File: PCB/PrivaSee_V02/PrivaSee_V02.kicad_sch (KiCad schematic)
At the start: 35 parts, among them J1 RFPC-SMA27-F, J2 Batt_Solder_Point, J3 Conn_02x06_Odd_Even, J4 VOUT_TEST, J5 GND_TEST, J6 IR_TEST, J7 RF_TEST, SW1 Switch, U1 RC1602A, U2 LM358, U3 254, U4 DFR0568, U6 ESP32-C5-DevKitC-1

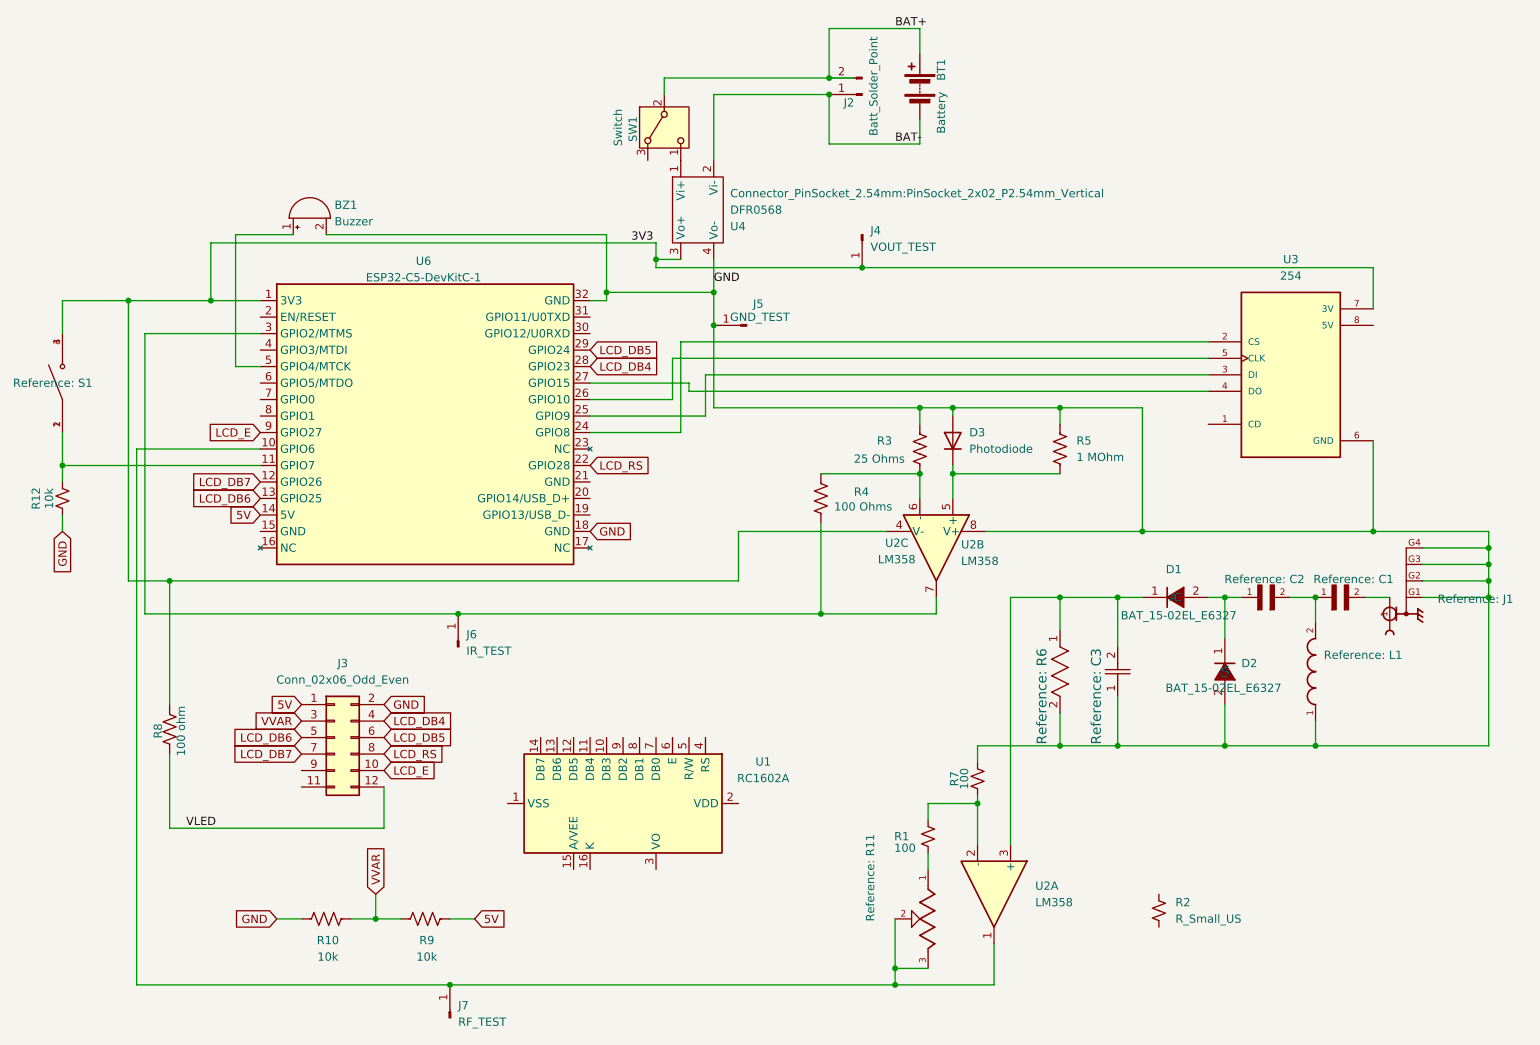
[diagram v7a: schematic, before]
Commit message: LM358 change
Our current schematic has the symbols for V- and V+ swapped. Ground and power are now routed and traced properly
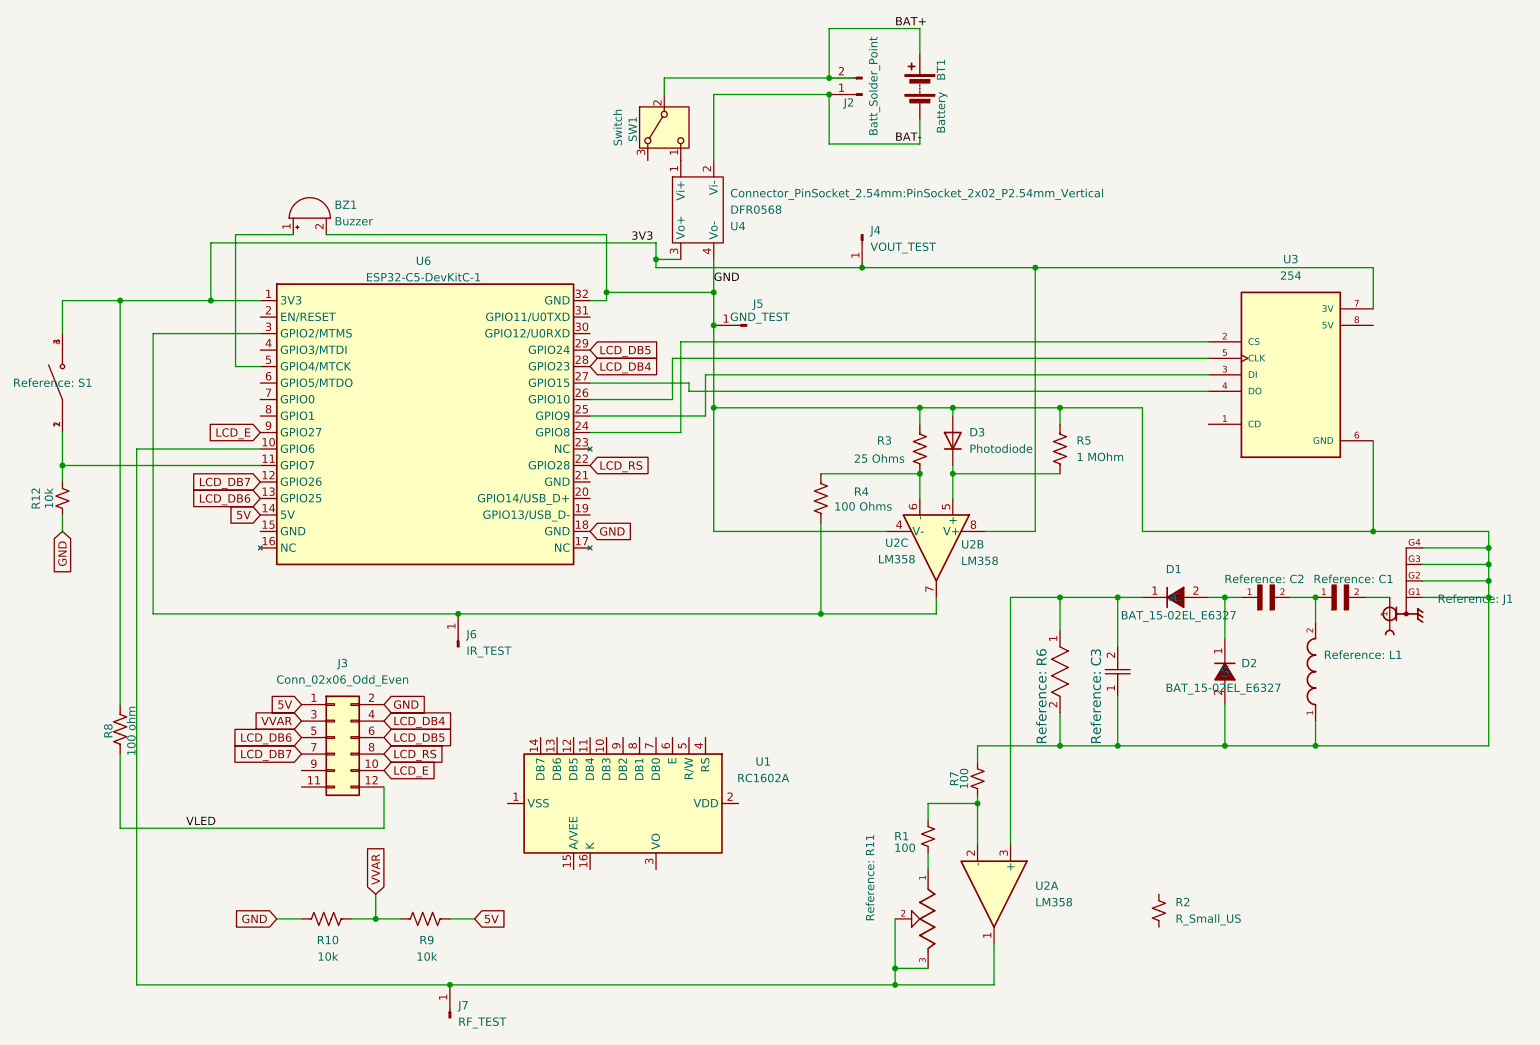
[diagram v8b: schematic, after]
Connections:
- net 3V3: now also U2.8 (V+); no longer U2.4 (V-)
- net GND: now also U2.4 (V-); no longer U2.8 (V+)
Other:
- moved on the sheet: R8
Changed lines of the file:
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@@
 	)
 	(junction
-		(at 95.25 105.41)
-		(diameter 0)
-		(color 0 0 0 0)
-	)
-	(junction
 		(at 118.11 55.88)
 		(diameter 0)
@@
 	)
 	(junction
-		(at 50.8 100.33)
-		(diameter 0)
-		(color 0 0 0 0)
-	)
-	(junction
 		(at 236.22 92.71)
 		(diameter 0)
@@
 	)
 	(junction
-		(at 151.13 105.41)
+		(at 184.15 52.07)
 		(diameter 0)
 		(color 0 0 0 0)
 	)
 	(junction
-		(at 152.4 25.4)
+		(at 151.13 105.41)
 		(diameter 0)
 		(color 0 0 0 0)
 	)
 	(junction
-		(at 200.66 92.71)
+		(at 152.4 25.4)
 		(diameter 0)
 		(color 0 0 0 0)
@@
 	)
 	(junction
-		(at 44.45 57.15)
+		(at 134.62 73.66)
 		(diameter 0)
 		(color 0 0 0 0)
@@
 	)
 	(junction
+		(at 43.18 57.15)
+		(diameter 0)
+		(color 0 0 0 0)
+	)
+	(junction
 		(at 162.56 160.02)
 		(diameter 0)
@@
 	)
 	(junction
+		(at 95.25 105.41)
+		(diameter 0)
+		(color 0 0 0 0)
+	)
+	(junction
 		(at 213.36 125.73)
 		(diameter 0)
@@
 	(wire
 		(pts
-			(xy 44.45 57.15) (xy 44.45 100.33)
+			(xy 43.18 57.15) (xy 43.18 119.38)
 		)
 		(stroke
@@
 	(wire
 		(pts
-			(xy 46.99 62.23) (xy 46.99 105.41)
+			(xy 184.15 92.71) (xy 176.53 92.71)
 		)
 		(stroke
@@
 	(wire
 		(pts
-			(xy 157.48 52.07) (xy 236.22 52.07)
+			(xy 48.26 62.23) (xy 48.26 105.41)
+		)
+		(stroke
+			(width 0)
+			(type default)
+		)
+	)
+	(wire
+		(pts
+			(xy 157.48 52.07) (xy 184.15 52.07)
 		)
 		(stroke
@@
 	(wire
 		(pts
-			(xy 213.36 102.87) (xy 215.9 102.87)
+			(xy 184.15 52.07) (xy 236.22 52.07)
 		)
 		(stroke
@@
 	(wire
 		(pts
-			(xy 34.29 57.15) (xy 34.29 62.23)
+			(xy 213.36 102.87) (xy 215.9 102.87)
 		)
 		(stroke
@@
 	(wire
 		(pts
-			(xy 175.26 125.73) (xy 175.26 128.27)
+			(xy 34.29 57.15) (xy 34.29 62.23)
 		)
 		(stroke
@@
 	(wire
 		(pts
-			(xy 44.45 100.33) (xy 138.43 100.33)
+			(xy 175.26 125.73) (xy 175.26 128.27)
 		)
 		(stroke
@@
 	(wire
 		(pts
-			(xy 138.43 100.33) (xy 138.43 92.71)
-		)
-		(stroke
-			(width 0)
-			(type default)
-		)
-	)
-	(wire
-		(pts
 			(xy 83.82 138.43) (xy 83.82 132.08)
 		)
@@
 	(wire
 		(pts
-			(xy 50.8 138.43) (xy 50.8 127)
-		)
-		(stroke
-			(width 0)
-			(type default)
-		)
-	)
-	(wire
-		(pts
-			(xy 46.99 105.41) (xy 95.25 105.41)
+			(xy 43.18 138.43) (xy 43.18 127)
 		)
 		(stroke
@@
 	(wire
 		(pts
-			(xy 50.8 100.33) (xy 50.8 119.38)
+			(xy 48.26 105.41) (xy 95.25 105.41)
 		)
 		(stroke
@@
 	(wire
 		(pts
-			(xy 46.99 62.23) (xy 64.77 62.23)
+			(xy 184.15 52.07) (xy 184.15 92.71)
 		)
 		(stroke
@@
 	(wire
 		(pts
-			(xy 82.55 148.59) (xy 82.55 152.4)
+			(xy 48.26 62.23) (xy 64.77 62.23)
 		)
 		(stroke
@@
 	(wire
 		(pts
-			(xy 130.81 69.85) (xy 115.57 69.85)
+			(xy 82.55 148.59) (xy 82.55 152.4)
 		)
 		(stroke
@@
 	(wire
 		(pts
-			(xy 254 92.71) (xy 236.22 92.71)
+			(xy 130.81 69.85) (xy 115.57 69.85)
 		)
 		(stroke
@@
 	(wire
 		(pts
-			(xy 254 92.71) (xy 254 95.25)
+			(xy 254 92.71) (xy 236.22 92.71)
 		)
 		(stroke
@@
 	(wire
 		(pts
-			(xy 175.26 134.62) (xy 175.26 140.97)
+			(xy 254 92.71) (xy 254 95.25)
 		)
 		(stroke
@@
 	(wire
 		(pts
-			(xy 187.96 107.95) (xy 187.96 102.87)
+			(xy 175.26 134.62) (xy 175.26 140.97)
 		)
 		(stroke
@@
 	(wire
 		(pts
-			(xy 176.53 92.71) (xy 200.66 92.71)
+			(xy 187.96 107.95) (xy 187.96 102.87)
 		)
 		(stroke
@@
 	(wire
 		(pts
-			(xy 50.8 138.43) (xy 83.82 138.43)
+			(xy 43.18 138.43) (xy 83.82 138.43)
 		)
 		(stroke
@@
 	(wire
 		(pts
-			(xy 254 100.33) (xy 254 102.87)
+			(xy 134.62 73.66) (xy 134.62 92.71)
 		)
 		(stroke
@@
 	(wire
 		(pts
-			(xy 128.27 66.04) (xy 128.27 72.39)
+			(xy 254 100.33) (xy 254 102.87)
 		)
 		(stroke
@@
 	(wire
 		(pts
-			(xy 196.85 102.87) (xy 200.66 102.87)
+			(xy 128.27 66.04) (xy 128.27 72.39)
 		)
 		(stroke
@@
 	(wire
 		(pts
-			(xy 138.43 92.71) (xy 161.29 92.71)
+			(xy 196.85 102.87) (xy 200.66 102.87)
 		)
 		(stroke
@@
 	(wire
 		(pts
-			(xy 166.37 73.66) (xy 171.45 73.66)
+			(xy 43.18 57.15) (xy 57.15 57.15)
 		)
 		(stroke
@@
 	(wire
 		(pts
-			(xy 234.95 102.87) (xy 238.76 102.87)
+			(xy 166.37 73.66) (xy 171.45 73.66)
 		)
 		(stroke
@@
 	(wire
 		(pts
-			(xy 166.37 29.21) (xy 166.37 33.02)
+			(xy 234.95 102.87) (xy 238.76 102.87)
 		)
 		(stroke
@@
 	(wire
 		(pts
-			(xy 34.29 57.15) (xy 44.45 57.15)
+			(xy 166.37 29.21) (xy 166.37 33.02)
 		)
 		(stroke
@@
 	(wire
 		(pts
-			(xy 152.4 33.02) (xy 152.4 25.4)
+			(xy 34.29 57.15) (xy 43.18 57.15)
 		)
 		(stroke
@@
 	(wire
 		(pts
-			(xy 93.98 152.4) (xy 97.79 152.4)
+			(xy 152.4 33.02) (xy 152.4 25.4)
 		)
 		(stroke
@@
 	(wire
 		(pts
-			(xy 213.36 109.22) (xy 213.36 102.87)
+			(xy 93.98 152.4) (xy 97.79 152.4)
 		)
 		(stroke
@@
 	(wire
 		(pts
-			(xy 254 97.79) (xy 254 100.33)
+			(xy 213.36 109.22) (xy 213.36 102.87)
 		)
 		(stroke
@@
 	(wire
 		(pts
-			(xy 236.22 92.71) (xy 200.66 92.71)
+			(xy 254 97.79) (xy 254 100.33)
 		)
 		(stroke
@@
 	(wire
 		(pts
+			(xy 134.62 92.71) (xy 161.29 92.71)
+		)
+		(stroke
+			(width 0)
+			(type default)
+		)
+	)
+	(wire
+		(pts
 			(xy 213.36 119.38) (xy 213.36 125.73)
 		)
@@
 	(wire
 		(pts
-			(xy 171.45 83.82) (xy 171.45 87.63)
+			(xy 200.66 92.71) (xy 236.22 92.71)
 		)
 		(stroke
@@
 	(wire
 		(pts
-			(xy 200.66 73.66) (xy 200.66 92.71)
+			(xy 171.45 83.82) (xy 171.45 87.63)
 		)
 		(stroke
@@
 	(wire
 		(pts
-			(xy 130.81 71.12) (xy 130.81 69.85)
+			(xy 200.66 73.66) (xy 200.66 92.71)
 		)
 		(stroke
@@
 	(wire
 		(pts
-			(xy 180.34 102.87) (xy 187.96 102.87)
+			(xy 130.81 71.12) (xy 130.81 69.85)
 		)
 		(stroke
@@
 	(wire
 		(pts
-			(xy 175.26 133.35) (xy 175.26 134.62)
+			(xy 180.34 102.87) (xy 187.96 102.87)
 		)
 		(stroke
@@
 	(wire
 		(pts
-			(xy 44.45 57.15) (xy 57.15 57.15)
+			(xy 175.26 133.35) (xy 175.26 134.62)
 		)
 		(stroke
@@
 	(symbol
 		(lib_id "Device:R_US")
-		(at 50.8 123.19 0)
+		(at 43.18 123.19 0)
 		(unit 1)
 		(body_style 1)
@@
 		(dnp no)
 		(property "Reference" "R8"
-			(at 49.022 123.444 90)
+			(at 41.402 123.444 90)
 			(show_name no)
 			(do_not_autoplace no)
@@
 		)
 		(property "Value" "100 ohm"
-			(at 52.578 123.444 90)
+			(at 44.958 123.444 90)
 			(show_name no)
 			(do_not_autoplace no)
@@
 		)
 		(property "Footprint" "Resistor_SMD:R_1206_3216Metric_Pad1.30x1.75mm_HandSolder"
-			(at 51.816 123.444 90)
+			(at 44.196 123.444 90)
 			(hide yes)
 			(show_name no)
@@
 		)
 		(property "Datasheet" ""
-			(at 50.8 123.19 0)
+			(at 43.18 123.19 0)
 			(hide yes)
 			(show_name no)
@@
 		)
 		(property "Description" "Resistor, US symbol"
-			(at 50.8 123.19 0)
+			(at 43.18 123.19 0)
 			(hide yes)
 			(show_name no)
